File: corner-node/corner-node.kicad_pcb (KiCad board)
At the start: 2 copper layers, 40 x 40 mm, 37 parts, among them IC1 LSM6DSV80XTR, J2 Conn_01x07, U3 LMR51430, U4 TCAN3404-Q1, Y1 ECS-250-10-47Q-CES-TR

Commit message: idk
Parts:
- moved C11 7.46 mm to (35.1, 79.7)
- moved C10 6.84 mm to (37.6, 79.7)
- moved C8 4.81 mm to (45.3, 80.9), turned to 180 degrees
- moved L1 4.24 mm to (41.1, 79.5), turned to 180 degrees
- moved R3 4.04 mm to (41.0, 74.7), turned to 90 degrees
- moved JP2 3.10 mm to (60.8, 95.8)
- moved JP3 3.10 mm to (62.5, 91.0)
- moved D2 2.09 mm to (41.1, 67.8), turned to 0 degrees
- moved R1 1.34 mm to (43.1, 74.7), turned to -90 degrees
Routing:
- net GND: track 53.9 -> 59.2 mm, vias 11 -> 14
- net Net-(U3-FB): track 9.20 -> 4.05 mm
- net /WHEEL_ID0: track 20.9 -> 17.8 mm
- net /WHEEL_ID1: track 20.3 -> 17.2 mm
- net 1_CAN-: track 9.61 -> 7.36 mm, vias 2 -> 0

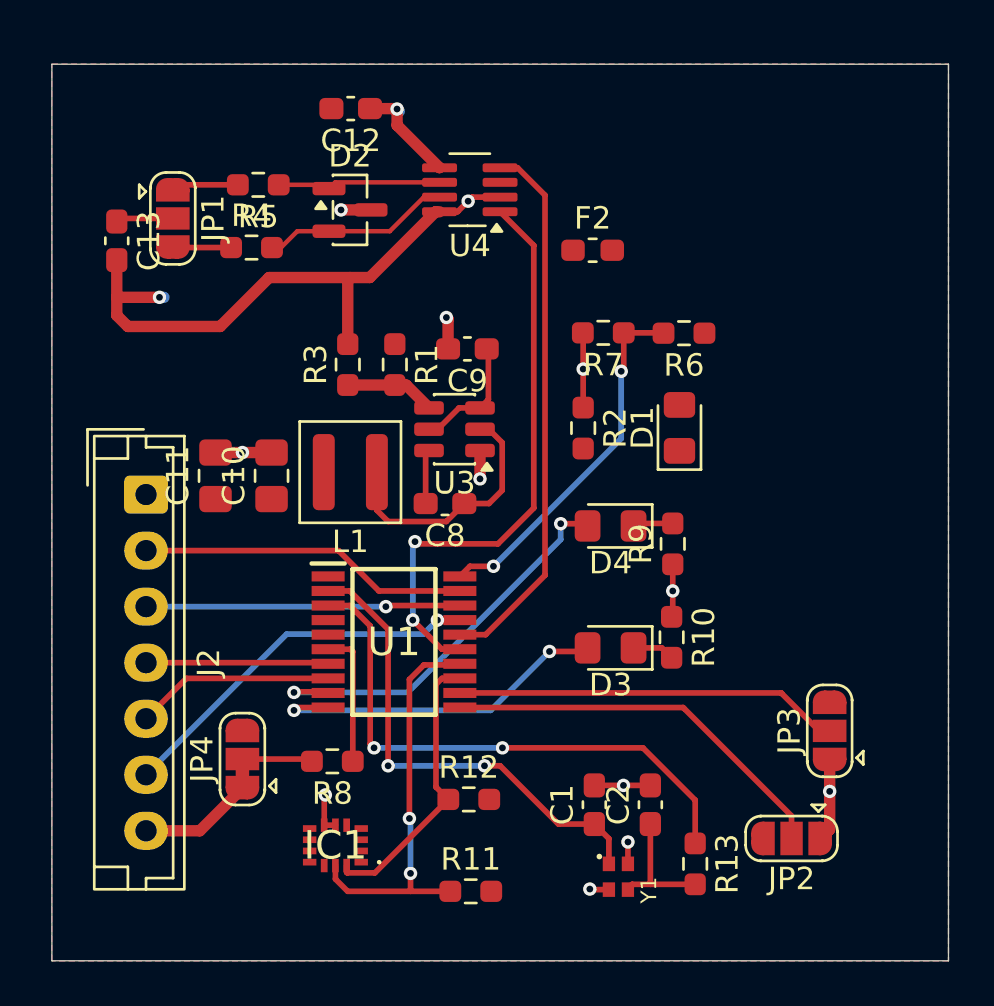
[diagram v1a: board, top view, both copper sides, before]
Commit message: more compact tm
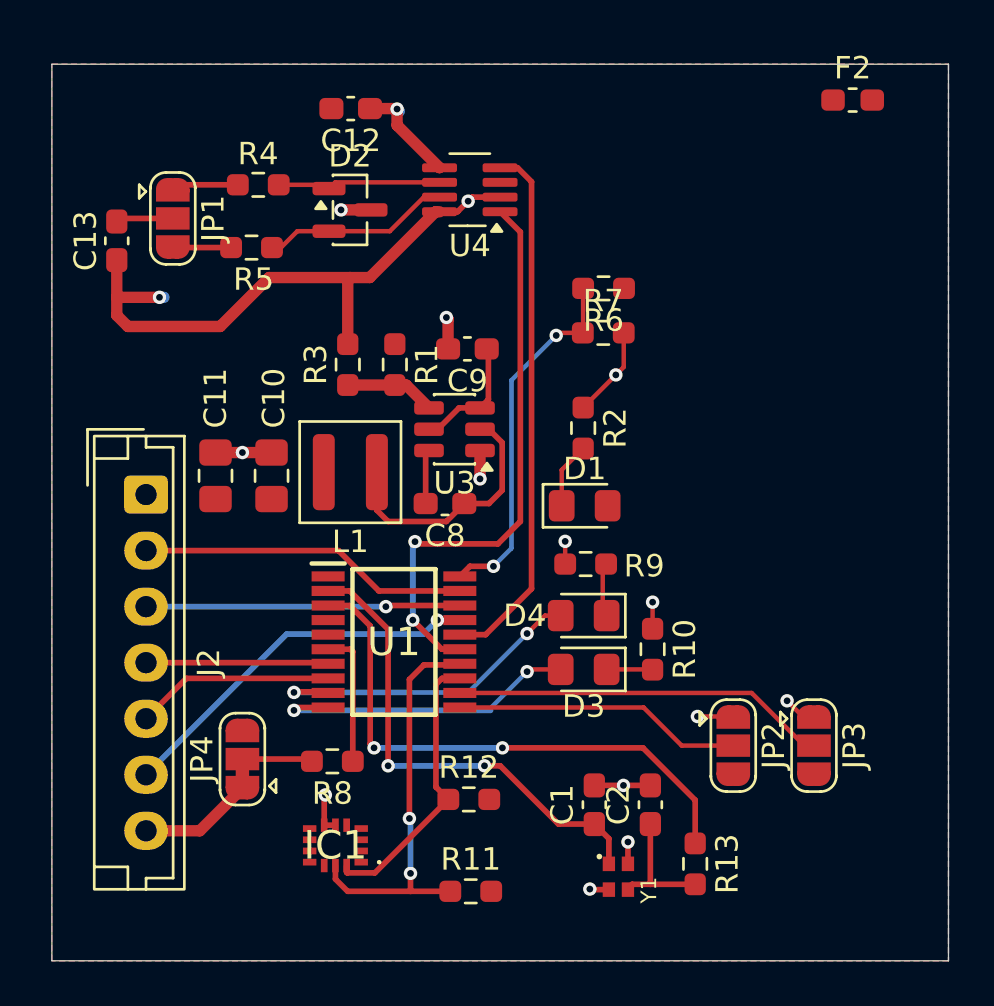
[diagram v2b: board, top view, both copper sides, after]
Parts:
- moved F2 13.4 mm to (63.5, 62.9)
- moved D1 5.47 mm to (51.6, 81.0), turned to 0 degrees
- moved JP2 4.89 mm to (58.2, 91.7), turned to -90 degrees
- moved D4 4.18 mm to (51.5, 85.9)
- moved R6 4.11 mm to (52.4, 71.3)
- moved R9 3.99 mm to (51.6, 83.6), turned to 0 degrees
- moved D3 1.54 mm to (51.5, 88.3)
- moved R10 1.00 mm to (54.6, 87.4)
- moved JP3 0.96 mm to (61.8, 91.7), turned to -90 degrees
- turned R7 to 0 degrees
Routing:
- net /WHEEL_ID0: track 17.8 -> 12.9 mm
- net /STATUS1_LED: track 18.0 -> 14.9 mm
- net Net-(D1-K): track 0.00 -> 2.95 mm
- net /ERROR_LED: track 15.8 -> 14.3 mm
- net GND: track 59.2 -> 59.4 mm, vias 14 -> 16

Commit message: idk
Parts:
- moved F2 12.3 mm to (52.5, 68.3)
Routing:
- net +GLV_PROT: track 5.22 -> 27.9 mm, vias 0 -> 2
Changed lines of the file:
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@@
 	(footprint "Fuse:Fuse_0603_1608Metric_Pad1.05x0.95mm_HandSolder"
 		(layer "F.Cu")
-		(at 63.525 62.9)
+		(at 52.5 68.3)
 		(descr "Fuse SMD 0603 (1608 Metric), square (rectangular) end terminal, IPC-7351 nominal with elongated pad for handsoldering. (Body size source: http://www.tortai-tech.com/upload/download/2011102023233369053.pdf), generated with kicad-footprint-generator")
 		(tags "fuse handsolder")
@@
 	)
 	(segment
-		(start 45.966236 76.633764)
-		(end 45.016236 77.583764)
-		(width 0.254)
+		(start 52.595 81)
+		(end 54.2665 79.3285)
+		(width 0.508)
+		(layer "F.Cu")
+		(net 6)
+	)
+	(segment
+		(start 51.79701 68.3)
+		(end 51.625 68.3)
+		(width 0.508)
 		(layer "F.Cu")
 		(net 6)
@@
 	(segment
 		(start 46.9 76.633764)
-		(end 47.275 76.258764)
-		(width 0.254)
+		(end 46.145842 76.633764)
+		(width 0.508)
 		(layer "F.Cu")
 		(net 6)
 	)
 	(segment
-		(start 47.275 76.258764)
-		(end 47.275 74.233764)
-		(width 0.254)
+		(start 46.9 74.3)
+		(end 47.2 74)
+		(width 0.508)
+		(layer "F.Cu")
+		(net 6)
+	)
+	(segment
+		(start 46.145842 76.633764)
+		(end 45.195842 77.583764)
+		(width 0.508)
+		(layer "F.Cu")
+		(net 6)
+	)
+	(segment
+		(start 47.2 74)
+		(end 47.2 72.2)
+		(width 0.508)
+		(layer "F.Cu")
+		(net 6)
+	)
+	(segment
+		(start 54.2665 70.76949)
+		(end 51.79701 68.3)
+		(width 0.508)
+		(layer "F.Cu")
+		(net 6)
+	)
+	(segment
+		(start 51.1 68.3)
+		(end 50 69.4)
+		(width 0.508)
+		(layer "F.Cu")
+		(net 6)
+	)
+	(segment
+		(start 54.2665 79.3285)
+		(end 54.2665 70.76949)
+		(width 0.508)
+		(layer "F.Cu")
+		(net 6)
+	)
+	(segment
+		(start 47.2 72.2)
+		(end 47.6 71.8)
+		(width 0.508)
 		(layer "F.Cu")
 		(net 6)
@@
 	(segment
 		(start 46.9 76.633764)
-		(end 45.966236 76.633764)
-		(width 0.254)
+		(end 46.9 74.3)
+		(width 0.508)
 		(layer "F.Cu")
 		(net 6)
 	)
 	(segment
-		(start 45.016236 77.583764)
+		(start 51.625 68.3)
+		(end 51.1 68.3)
+		(width 0.508)
+		(layer "F.Cu")
+		(net 6)
+	)
+	(segment
+		(start 45.195842 77.583764)
 		(end 44.625 77.583764)
-		(width 0.254)
+		(width 0.508)
 		(layer "F.Cu")
 		(net 6)
 	)
+	(via
+		(at 47.6 71.8)
+		(size 0.6)
+		(drill 0.3)
+		(layers "F.Cu" "B.Cu")
+		(net 6)
+	)
+	(via
+		(at 50 69.4)
+		(size 0.6)
+		(drill 0.3)
+		(layers "F.Cu" "B.Cu")
+		(net 6)
+	)
+	(segment
+		(start 47.6 71.8)
+		(end 50 69.4)
+		(width 0.508)
+		(layer "B.Cu")
+		(net 6)
+	)

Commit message: odsohflsiadhflashdfilh
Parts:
- moved R13 21.7 mm to (38.0, 85.7), turned to 90 degrees
- moved C2 21.7 mm to (35.5, 83.8), turned to 0 degrees
- moved Y1 21.0 mm to (35.7, 85.8), turned to 90 degrees
- moved C1 17.6 mm to (35.6, 87.8), turned to 180 degrees
- moved JP2 8.52 mm to (50.7, 95.8)
- moved JP3 8.52 mm to (54.3, 95.8)
- moved U3 1.89 mm to (46.1, 79.5), turned to 0 degrees
- moved C8 1.30 mm to (46.2, 81.9), turned to 0 degrees
- moved J2 0.80 mm to (31.2, 80.5)
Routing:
- net /RCC_OSCX_OUT: track 25.0 -> 2.70 mm, vias 2 -> 0
- net /RCC_OSCX_IN: track 21.8 -> 6.36 mm, vias 2 -> 0
- net Net-(U3-SW): track 11.4 -> 3.90 mm
- net /WHEEL_ID1: track 16.8 -> 11.0 mm
- net GND: track 59.4 -> 65.2 mm, vias 16 -> 15
- net Net-(U3-FB): track 4.05 -> 9.33 mm, vias 0 -> 2
- net /WHEEL_ID0: track 12.9 -> 8.43 mm
- net +GLV_PROT: track 27.9 -> 32.0 mm
- net /STATUS1_LED: track 14.9 -> 11.8 mm
- net /ERROR_LED: track 14.3 -> 11.2 mm
- net /DEBUG_SWDIO: track 14.0 -> 16.6 mm, vias 1 -> 0
- net Net-(U3-CB): track 2.43 -> 4.66 mm
- net /BOOT0: track 6.04 -> 7.75 mm
- net /DEBUG_SWCLK: track 14.7 -> 15.7 mm
- net /USART1_TX: track 8.14 -> 8.93 mm
- added copper zone on F.Cu, net Net-(U3-SW)
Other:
- outline, holes or cut-outs redrawn

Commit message: changes
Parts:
- added J1: Conn_01x06, Connector_Molex:Molex_Micro-Fit_3.0_43045-0610_2x03-1MP_P3.00mm_Horizontal, F.Cu at (54.7, 70.3)
- moved R6 9.53 mm to (58.3, 78.8)
- moved R7 9.40 mm to (58.3, 80.6)
- moved F2 4.21 mm to (54.5, 64.6)
- moved C1 0.10 mm to (35.5, 87.8)
- turned D1 to 180 degrees
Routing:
- net /PPS_IN: track 0.00 -> 24.8 mm, vias 0 -> 2
- net 1_CAN+: track 8.41 -> 19.6 mm
- net /WHEELSPEED sensor: track 0.00 -> 9.42 mm
- net 1_CAN-: track 7.36 -> 16.6 mm
- net Net-(J1-Pin_1): track 0.00 -> 3.37 mm
- net +3V3: track 0.00 -> 3.01 mm
- net GND: track 65.2 -> 62.6 mm, vias 15 -> 17
- net /WHEELSPEED IN: track 16.4 -> 15.4 mm
- net /FDCAN1_TX: track 25.5 -> 24.9 mm
- net +GLV_PROT: track 32.0 -> 31.4 mm, vias 2 -> 4
